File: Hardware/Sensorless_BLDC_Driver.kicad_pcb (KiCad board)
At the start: 2 copper layers, 67.5 x 67.5 mm, 76 parts, among them J1 POWER, J2 MOTOR, Q1 BUK7M15-60EX, Q2 BUK7M15-60EX, Q3 BUK7M15-60EX, Q4 BUK7M15-60EX, Q5 BUK7M15-60EX, Q6 BUK7M15-60EX, U1 PSoC5LP_Prototyping_Kit, U2 FAN7888

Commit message: PCB chotto susunda
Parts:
- added J3: Encoder, KUTKiCad_footprint:Hirose_DF1E_DF1E-5P-2.5DS_1x05_P2.5mm_Vertical, F.Cu at (207.4, 34.3)
- added RV1: 10k, Potentiometer_THT:Potentiometer_Alps_RK09K_Single_Vertical, F.Cu at (201.0, 46.7)
- added RV2: 10k, Potentiometer_THT:Potentiometer_Alps_RK09K_Single_Vertical, F.Cu at (216.1, 38.1)
- J1: footprint Connector_Hirose:Hirose_DF63M-2P-3.96DSA_1x02_P3.96mm_Vertical -> KUTKiCad_footprint:Hirose_DF22_DF22x-2P-7.92DSA_1x02_P7.92mm_Vertical
- J2: footprint Connector_Hirose:Hirose_DF63M-3P-3.96DSA_1x03_P3.96mm_Vertical -> KUTKiCad_footprint:Hirose_DF22_DF22x-3P-7.92DSA_1x03_P7.92mm_Vertical
- moved C15 35.4 mm to (241.4, 139.2)
- moved C17 35.4 mm to (241.4, 122.9)
- moved C16 35.4 mm to (241.4, 131.0)
- moved Q6 29.2 mm to (217.1, 104.1)
- moved Q5 28.9 mm to (217.1, 100.3)
- moved R5 27.0 mm to (246.7, 115.1)
- moved R6 27.0 mm to (244.2, 115.1)
- moved R7 27.0 mm to (241.6, 115.1)
- moved R8 27.0 mm to (239.1, 115.1)
- moved J2 15.3 mm to (226.7, 111.7), turned to 270 degrees
- moved Q4 13.5 mm to (217.1, 111.7)
- moved Q3 13.3 mm to (217.1, 107.9)
- moved U2 9.30 mm to (211.2, 89.6), turned to 90 degrees
- moved R10 8.98 mm to (197.5, 107.5)
- moved D2 8.98 mm to (199.3, 103.7)
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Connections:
- J2 pad 1: MOTOR_W -> MOTOR_U
- J2 pad 3: MOTOR_U -> MOTOR_W
- U1 pad 1: Net-(U1-Pad1) -> +5V
- U1 pad 10: Net-(U1-Pad10) -> /POT_2
- U1 pad 11: Net-(U1-Pad11) -> /POT_1
- U1 pad 38: Net-(U1-Pad38) -> /Index
- U1 pad 39: Net-(U1-Pad39) -> /Ch_B
- U1 pad 40: Net-(U1-Pad40) -> /Ch_A
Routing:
- net MOTOR_W: track 39.6 -> 0.00 mm, vias 1 -> 0
- net Net-(Q6-Pad4): track 38.0 -> 0.00 mm, vias 2 -> 0
- net Net-(Q5-Pad4): track 35.3 -> 0.00 mm, vias 2 -> 0
- net MOTOR_V: track 28.9 -> 0.00 mm, vias 1 -> 0
- net Net-(Q4-Pad4): track 24.2 -> 0.00 mm, vias 2 -> 0
- net /VB1: track 22.8 -> 0.00 mm
- net MOTOR_U: track 20.2 -> 0.00 mm
- net Net-(Q3-Pad4): track 17.7 -> 0.04 mm, vias 2 -> 0
- net /VB2: track 11.9 -> 0.00 mm
- net /VB3: track 9.92 -> 0.00 mm
- net Net-(Q2-Pad4): track 9.37 -> 0.00 mm, vias 2 -> 0
- net Net-(R11-Pad1): track 5.32 -> 0.00 mm, vias 40 -> 0
- net VDD: track 4.80 -> 0.00 mm, vias 93 -> 72
- net Net-(Q6-Pad1): track 1.80 -> 0.00 mm
- net Net-(Q4-Pad1): track 1.80 -> 0.00 mm
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- removed copper zone on F.Cu, net Net-(Q2-Pad1)
- removed copper zone on F.Cu, net Net-(Q4-Pad1)
- removed copper zone on F.Cu, net Net-(Q6-Pad1)
- removed copper zone on B.Cu, net Net-(R11-Pad1)
- removed copper zone on F.Cu, net Net-(R11-Pad1)
- removed copper zone on B.Cu, net VDD
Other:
- board size 67.5 x 67.5 mm -> 70 x 70 mm

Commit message: [update] PCB pattern complete
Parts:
- removed C18: 0.1u, Capacitor_SMD:C_0402_1005Metric
- removed R34: 120, Resistor_SMD:R_0402_1005Metric
- removed R35: 33k, Resistor_SMD:R_0402_1005Metric
- removed R36: 10k, Resistor_SMD:R_0402_1005Metric
- removed TP1: BEMF1, TestPoint:TestPoint_THTPad_D1.0mm_Drill0.5mm
- removed TP2: BEMF2, TestPoint:TestPoint_THTPad_D1.0mm_Drill0.5mm
- removed TP3: BEMF3, TestPoint:TestPoint_THTPad_D1.0mm_Drill0.5mm
- removed TP4: BEMFN, TestPoint:TestPoint_THTPad_D1.0mm_Drill0.5mm
- R20: value 2m -> 120; footprint Resistor_SMD:R_0805_2012Metric -> Resistor_SMD:R_0402_1005Metric
- R21, R22: value 4.7 -> 120
- R32: value 120 -> 33k
- R33: value 120 -> 10k
- moved D1 136.4 mm to (222.7, 149.8), turned to 90 degrees
- moved R1 131.5 mm to (222.7, 146.7), turned to 90 degrees
- moved C3 115.6 mm to (216.0, 130.8), turned to 180 degrees
- moved R33 113.0 mm to (204.4, 143.8), turned to 180 degrees
- moved R32 111.8 mm to (204.4, 142.3), turned to 180 degrees
- moved J3 111.8 mm to (170.3, 139.7), turned to 90 degrees
- moved C5 111.1 mm to (223.0, 99.3), turned to 90 degrees
- moved R31 108.0 mm to (204.0, 137.0), turned to 180 degrees
- moved R30 107.0 mm to (204.0, 134.4), turned to 180 degrees
- moved R24 106.6 mm to (206.0, 128.3), turned to 270 degrees
- moved R25 106.3 mm to (208.2, 128.3), turned to 270 degrees
- moved C14 106.1 mm to (200.4, 137.4), turned to 90 degrees
- moved C13 105.3 mm to (200.4, 134.9), turned to 90 degrees
- moved R28 105.3 mm to (207.1, 128.3), turned to 270 degrees
- moved R29 104.7 mm to (204.0, 131.9), turned to 180 degrees
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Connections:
- C11 pad 1: /ISL -> GND
- C11 pad 2: /ISH -> /VS
- R11 pad 1: Net-(R11-Pad1) -> GND
- R13 pad 1: Net-(R11-Pad1) -> GND
- R14 pad 1: Net-(R11-Pad1) -> GND
- R16 pad 1: Net-(R11-Pad1) -> GND
- R17 pad 1: Net-(R11-Pad1) -> GND
- R19 pad 1: Net-(R11-Pad1) -> GND
- R20 pad 1: GND -> Net-(R20-Pad1)
- R20 pad 2: Net-(R11-Pad1) -> /BEMF1
- R21 pad 1: Net-(R11-Pad1) -> Net-(R21-Pad1)
- R21 pad 2: /ISH -> /BEMF2
- R22 pad 1: GND -> Net-(R22-Pad1)
- R22 pad 2: /ISL -> /BEMF3
- R23 pad 2: Net-(R23-Pad2) -> Net-(R20-Pad1)
- R24 pad 2: Net-(R24-Pad2) -> Net-(R21-Pad1)
- R25 pad 2: Net-(R25-Pad2) -> Net-(R22-Pad1)
- R26 pad 2: Net-(R23-Pad2) -> Net-(R20-Pad1)
- R27 pad 2: Net-(R24-Pad2) -> Net-(R21-Pad1)
- R28 pad 2: Net-(R25-Pad2) -> Net-(R22-Pad1)
- R29 pad 2: Net-(R23-Pad2) -> /BEMF1
- R30 pad 2: Net-(R24-Pad2) -> /BEMF2
- R31 pad 2: Net-(R25-Pad2) -> /BEMF3
- R32 pad 1: Net-(R23-Pad2) -> VDD
- R32 pad 2: /BEMF1 -> /VS
- R33 pad 1: Net-(R24-Pad2) -> GND
- R33 pad 2: /BEMF2 -> /VS
- U1 pad 10: /POT_2 -> /ISH_3
- U1 pad 11: /POT_1 -> /ISL_3
- U1 pad 12: /ISL_3 -> /ISH_2
- U1 pad 13: /ISH_3 -> /ISL_2
- U1 pad 14: /ISL_2 -> /ISL_1
- U1 pad 15: /ISH_2 -> /ISH_1
- U1 pad 16: /ISL_1 -> Net-(U1-Pad16)
- U1 pad 17: /ISH_1 -> Net-(U1-Pad17)
- U1 pad 18: /ISL -> Net-(U1-Pad18)
- U1 pad 19: /ISH -> /BEMF1
- U1 pad 20: Net-(U1-Pad20) -> /BEMF2
- U1 pad 21: Net-(U1-Pad21) -> /BEMF3
- U1 pad 22: Net-(U1-Pad22) -> /BEMF_N
- U1 pad 24: Net-(U1-Pad24) -> /VS
- U1 pad 27: Net-(U1-Pad27) -> /HIN_1
- U1 pad 28: Net-(U1-Pad28) -> /LIN_1
- U1 pad 29: Net-(U1-Pad29) -> /HIN_2
- U1 pad 30: Net-(U1-Pad30) -> /LIN_2
- U1 pad 31: /BEMF_N -> /HIN_3
- U1 pad 32: /BEMF3 -> /LIN_3
- U1 pad 33: /BEMF2 -> Net-(U1-Pad33)
- U1 pad 34: /BEMF1 -> /POT_1
- U1 pad 38: /Index -> Net-(U1-Pad38)
- U1 pad 39: /Ch_B -> Net-(U1-Pad39)
- U1 pad 40: /Ch_A -> Net-(U1-Pad40)
- U1 pad 43: /HIN_1 -> Net-(U1-Pad43)
- U1 pad 44: /LIN_1 -> Net-(U1-Pad44)
- U1 pad 45: /HIN_2 -> /POT_2
- U1 pad 46: /LIN_2 -> Net-(U1-Pad46)
- U1 pad 47: /HIN_3 -> /Index
- U1 pad 48: /LIN_3 -> /Ch_B
- U1 pad 49: Net-(U1-Pad49) -> /Ch_A
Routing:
- net +5V: track 0.00 -> 93.2 mm, vias 0 -> 1
- net MOTOR_W: track 0.00 -> 76.2 mm, vias 0 -> 1
- net MOTOR_V: track 0.00 -> 70.1 mm, vias 0 -> 1
- net MOTOR_U: track 0.00 -> 63.2 mm, vias 0 -> 1
- net /HIN_3: track 0.00 -> 57.9 mm
- net /LIN_3: track 0.00 -> 57.7 mm
- net /LIN_2: track 0.00 -> 57.6 mm
- net /HIN_2: track 0.00 -> 57.3 mm
- net /LIN_1: track 0.00 -> 56.9 mm
- net /HIN_1: track 0.00 -> 56.7 mm
- net VDD: track 0.00 -> 46.4 mm, vias 72 -> 53
- net Net-(Q2-Pad4): track 0.00 -> 31.5 mm, vias 0 -> 2
- net /VB1: track 0.00 -> 23.1 mm
- net Net-(Q1-Pad4): track 0.00 -> 21.0 mm, vias 0 -> 2
- net Net-(Q6-Pad4): track 0.00 -> 20.7 mm, vias 0 -> 2
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- added copper zone on B.Cu, net GND
- added copper zone on F.Cu, net GND
- added copper zone on F.Cu, net Net-(Q2-Pad1)
- added copper zone on F.Cu, net Net-(Q4-Pad1)
- added copper zone on F.Cu, net Net-(Q6-Pad1)
- added copper zone on B.Cu, net VDD
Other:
- board size 70 x 70 mm -> 75 x 75 mm

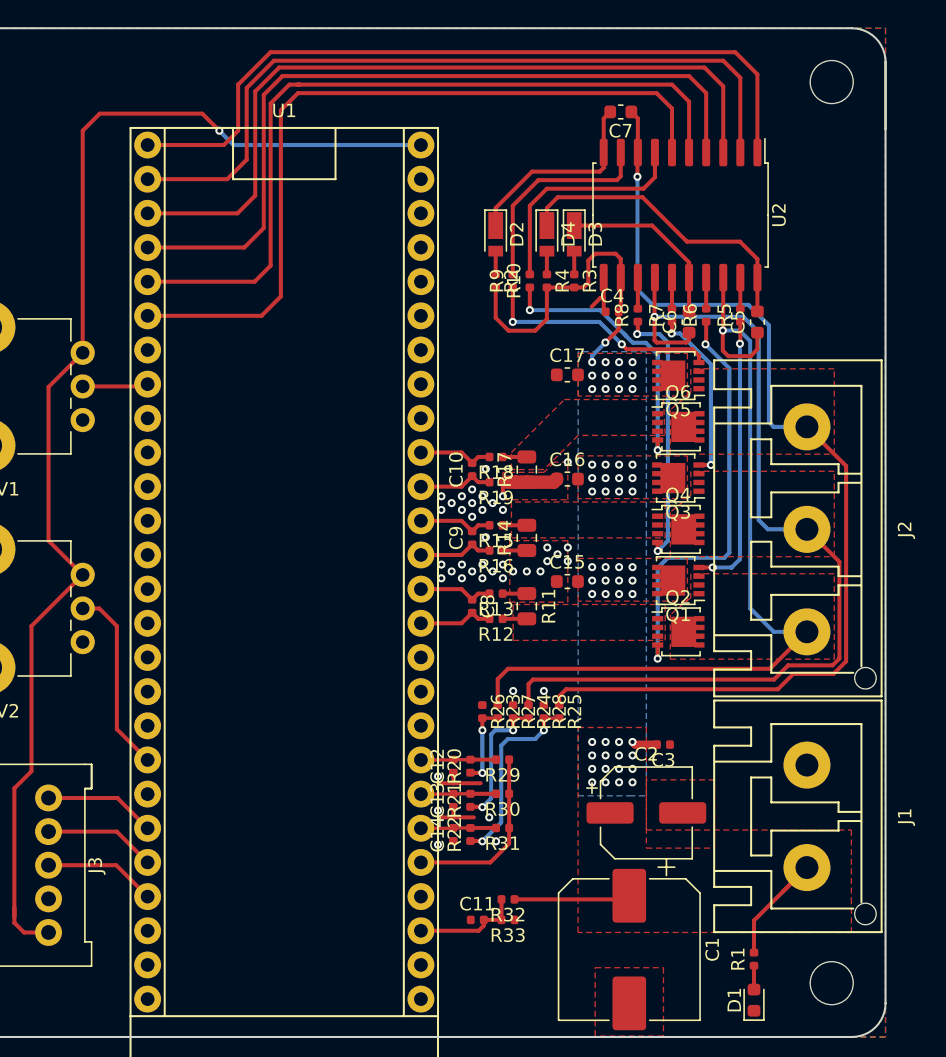
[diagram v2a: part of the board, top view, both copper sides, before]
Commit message: [update] adjust silk
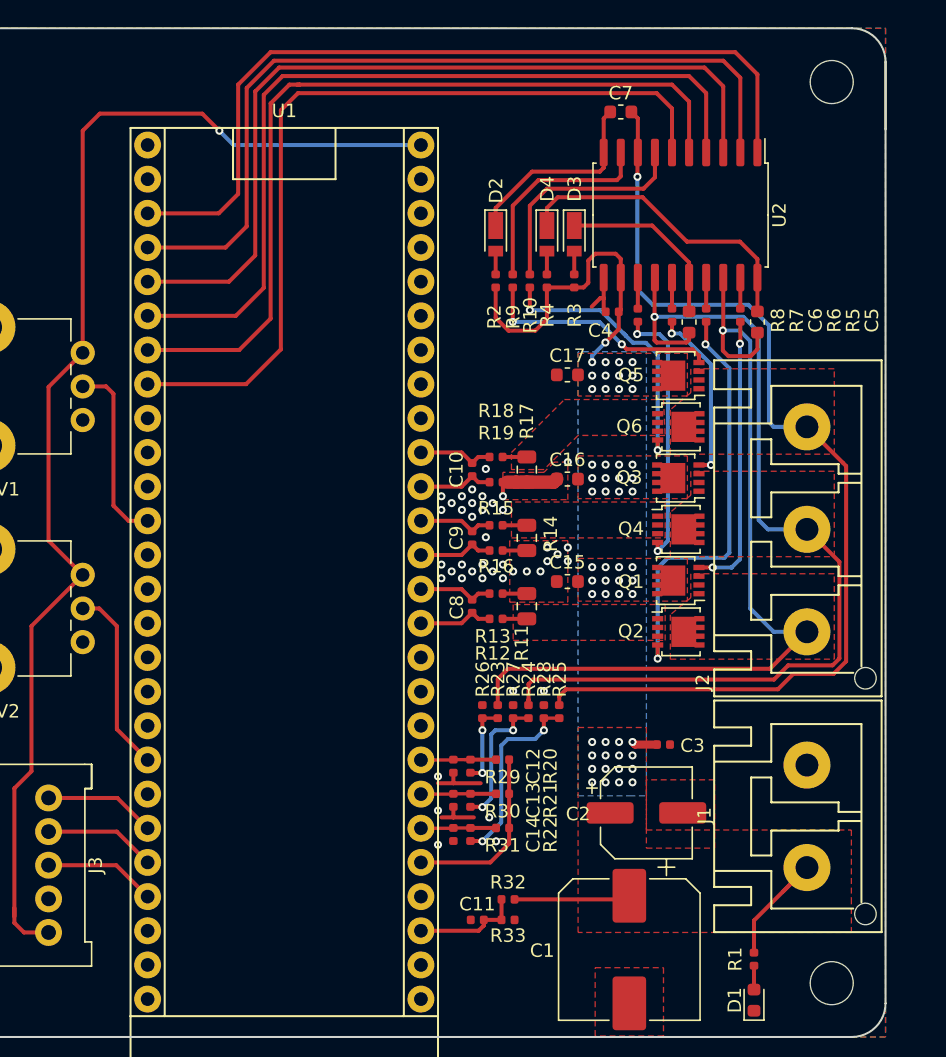
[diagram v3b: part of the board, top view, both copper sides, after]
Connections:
- U1 pad 27: /HIN_1 -> Net-(U1-Pad27)
- U1 pad 28: /LIN_1 -> Net-(U1-Pad28)
- U1 pad 29: /HIN_2 -> /HIN_1
- U1 pad 30: /LIN_2 -> /LIN_1
- U1 pad 31: /HIN_3 -> /HIN_2
- U1 pad 32: /LIN_3 -> /LIN_2
- U1 pad 33: Net-(U1-Pad33) -> /HIN_3
- U1 pad 34: /POT_1 -> /LIN_3
- U1 pad 38: Net-(U1-Pad38) -> /POT_1
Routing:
- net /POT_1: track 4.90 -> 13.8 mm
- net /LIN_1: track 56.9 -> 61.9 mm
- net /HIN_1: track 56.7 -> 61.6 mm
- net /LIN_2: track 57.6 -> 62.3 mm
- net /HIN_2: track 57.3 -> 62.0 mm
- net /LIN_3: track 57.7 -> 62.3 mm
- net /HIN_3: track 57.9 -> 62.3 mm

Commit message: [update] add via
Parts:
- added G***: LOGO, logo:niwatori, F.Cu at (167.0, 90.5)
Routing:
- net GND: vias 42 -> 201
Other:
- board text added: "Sensorless BLDC Motor Driver Rev.1 Designed by T.Niwa 2020.5"
